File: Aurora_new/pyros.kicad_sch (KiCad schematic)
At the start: 20 parts, among them J10 Screw_Terminal_01x02, J11 Screw_Terminal_01x02, J12 Screw_Terminal_01x04, J13 Screw_Terminal_01x02, J14 Screw_Terminal_01x02, J15 Screw_Terminal_01x02, J2 Screw_Terminal_01x04, J22 Screw_Terminal_01x08, J23 Screw_Terminal_01x08, J24 Screw_Terminal_01x08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

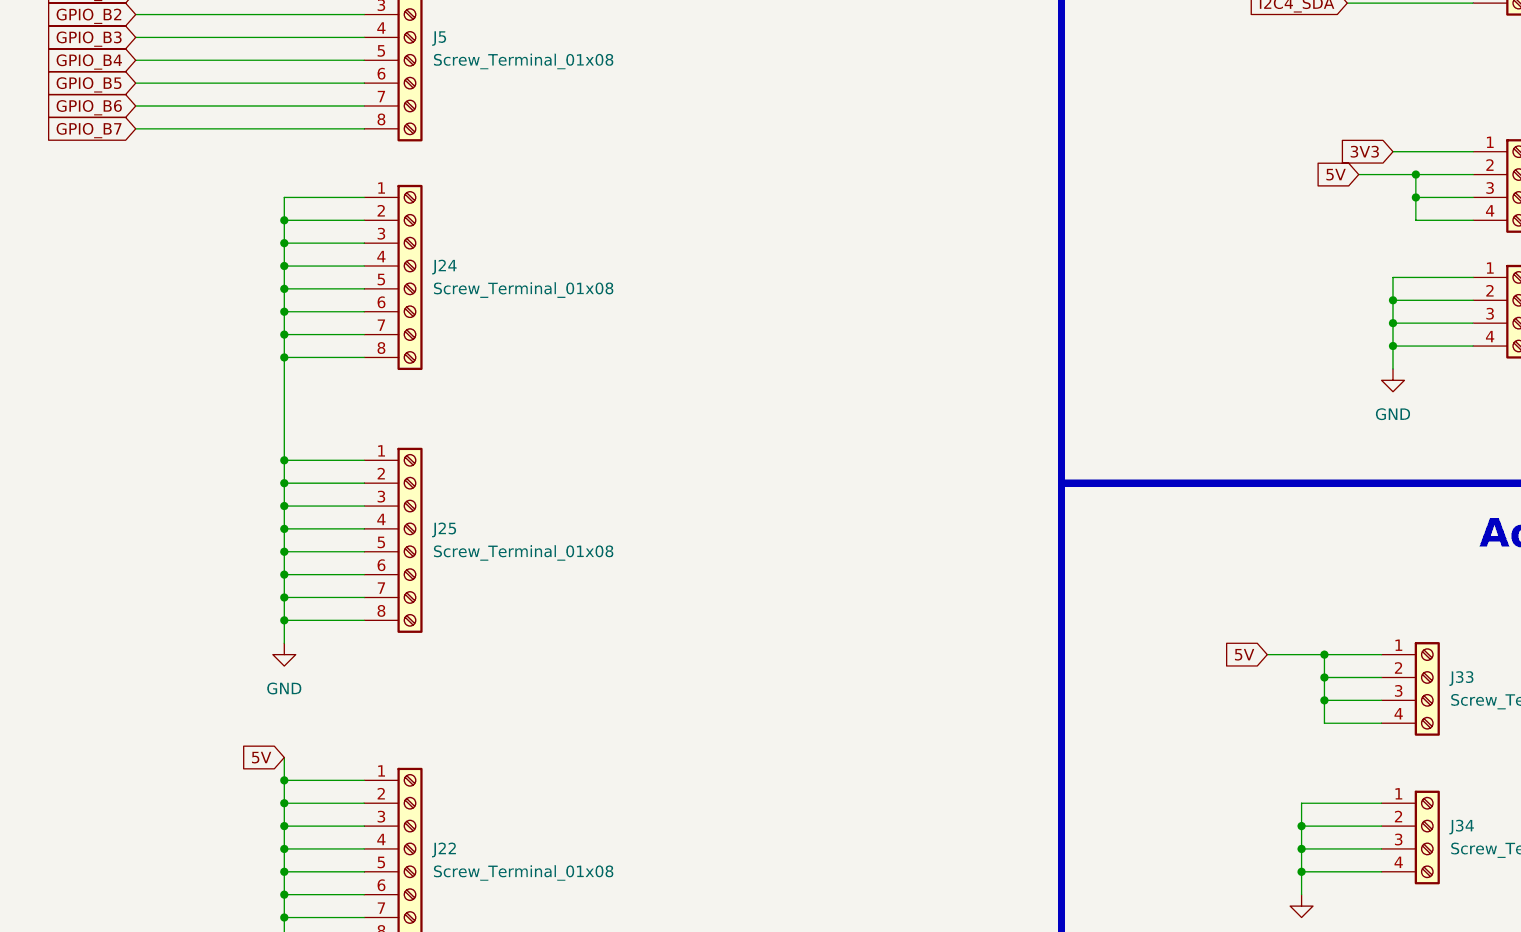
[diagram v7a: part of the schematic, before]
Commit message: fixed schematic issues, started organizing components in PCB
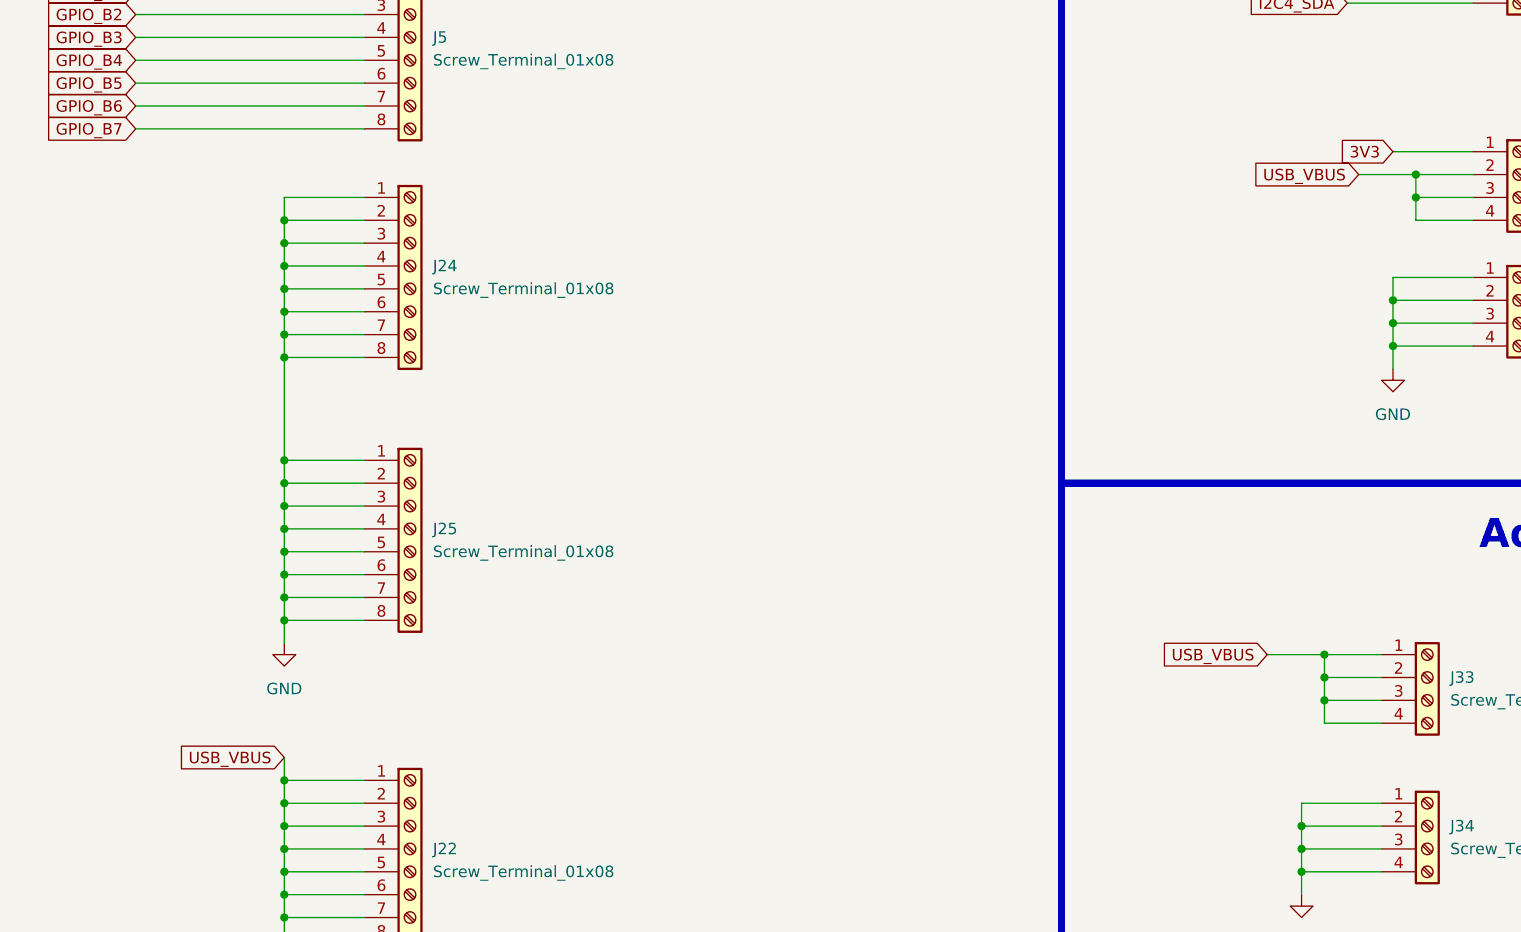
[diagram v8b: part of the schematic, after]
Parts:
- J10, J11, J13, J14, J15: footprint footprints5:CONN_1729128_PXC -> 1984617:PHOENIX_1984617
- J12, J2, J33, J34, J35, J7, J9: footprint footprints6:CONN_1715747_PXC -> 1984633:PHOENIX_1984633
- J22, J23, J24, J25, J4, J5: footprint footprints7:CONN_1715789_PXC -> 1984675:PHOENIX_1984675
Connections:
- net 5V renamed USB_VBUS
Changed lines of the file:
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@@
 		)
 	)
-	(global_label "5V"
+	(global_label "USB_VBUS"
 		(shape input)
 		(at 168.91 76.2 180)
@@
 		)
 		(property "Intersheetrefs" "${INTERSHEET_REFS}"
-			(at 163.6267 76.2 0)
+			(at 156.2486 76.2 0)
 			(effects
 				(font
@@
 		)
 	)
-	(global_label "5V"
+	(global_label "USB_VBUS"
 		(shape input)
 		(at 49.53 140.97 180)
@@
 		)
 		(property "Intersheetrefs" "${INTERSHEET_REFS}"
-			(at 44.2467 140.97 0)
+			(at 36.8686 140.97 0)
 			(effects
 				(font
@@
 		)
 	)
-	(global_label "5V"
+	(global_label "USB_VBUS"
 		(shape input)
 		(at 158.75 129.54 180)
@@
 		)
 		(property "Intersheetrefs" "${INTERSHEET_REFS}"
-			(at 153.4667 129.54 0)
+			(at 146.0886 129.54 0)
 			(effects
 				(font
@@
 			)
 		)
-		(property "Footprint" "footprints6:CONN_1715747_PXC"
+		(property "Footprint" "1984633:PHOENIX_1984633"
 			(at 256.54 53.34 0)
 			(effects
@@
 			)
 		)
-		(property "Footprint" "footprints6:CONN_1715747_PXC"
+		(property "Footprint" "1984633:PHOENIX_1984633"
 			(at 176.53 148.59 0)
 			(effects
@@
 			)
 		)
-		(property "Footprint" "footprints7:CONN_1715789_PXC"
+		(property "Footprint" "1984675:PHOENIX_1984675"
 			(at 63.5 60.96 0)
 			(effects
@@
 			)
 		)
-		(property "Footprint" "footprints7:CONN_1715789_PXC"
+		(property "Footprint" "1984675:PHOENIX_1984675"
 			(at 63.5 179.07 0)
 			(effects
@@
 			)
 		)
-		(property "Footprint" "footprints5:CONN_1729128_PXC"
+		(property "Footprint" "1984617:PHOENIX_1984617"
 			(at 186.69 54.61 0)
 			(effects
@@
 			)
 		)
-		(property "Footprint" "footprints6:CONN_1715747_PXC"
+		(property "Footprint" "1984633:PHOENIX_1984633"
 			(at 256.54 39.37 0)
 			(effects
@@
 			)
 		)
-		(property "Footprint" "footprints6:CONN_1715747_PXC"
+		(property "Footprint" "1984633:PHOENIX_1984633"
 			(at 186.69 76.2 0)
 			(effects
@@
 			)
 		)
-		(property "Footprint" "footprints7:CONN_1715789_PXC"
+		(property "Footprint" "1984675:PHOENIX_1984675"
 			(at 63.5 115.57 0)
 			(effects
@@
 			)
 		)
-		(property "Footprint" "footprints5:CONN_1729128_PXC"
+		(property "Footprint" "1984617:PHOENIX_1984617"
 			(at 186.69 36.83 0)
 			(effects
@@
 			)
 		)
-		(property "Footprint" "footprints7:CONN_1715789_PXC"
+		(property "Footprint" "1984675:PHOENIX_1984675"
 			(at 63.5 151.13 0)
 			(effects
@@
 			)
 		)
-		(property "Footprint" "footprints5:CONN_1729128_PXC"
+		(property "Footprint" "1984617:PHOENIX_1984617"
 			(at 256.54 92.71 0)
 			(effects
@@
 			)
 		)
-		(property "Footprint" "footprints6:CONN_1715747_PXC"
+		(property "Footprint" "1984633:PHOENIX_1984633"
 			(at 186.69 90.17 0)
 			(effects
@@
 			)
 		)
-		(property "Footprint" "footprints6:CONN_1715747_PXC"
+		(property "Footprint" "1984633:PHOENIX_1984633"
 			(at 176.53 132.08 0)
 			(effects
@@
 			)
 		)
-		(property "Footprint" "footprints7:CONN_1715789_PXC"
+		(property "Footprint" "1984675:PHOENIX_1984675"
 			(at 63.5 86.36 0)
 			(effects
@@
 			)
 		)
-		(property "Footprint" "footprints7:CONN_1715789_PXC"
+		(property "Footprint" "1984675:PHOENIX_1984675"
 			(at 63.5 35.56 0)
 			(effects
@@
 			)
 		)
-		(property "Footprint" "footprints5:CONN_1729128_PXC"
+		(property "Footprint" "1984617:PHOENIX_1984617"
 			(at 256.54 83.82 0)
 			(effects
@@
 			)
 		)
-		(property "Footprint" "footprints5:CONN_1729128_PXC"
+		(property "Footprint" "1984617:PHOENIX_1984617"
 			(at 186.69 45.72 0)
 			(effects
@@
 			)
 		)
-		(property "Footprint" "footprints6:CONN_1715747_PXC"
+		(property "Footprint" "1984633:PHOENIX_1984633"
 			(at 218.44 139.7 0)
 			(effects
